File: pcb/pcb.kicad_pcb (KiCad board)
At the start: 2 copper layers, 57 parts, among them J1 AMT0440007DB0000G, J10 Conn_02x10_Counter_Clockwise, J11 Conn_01x03, J12 Conn_01x02, J15 Conn_01x10, J16 Conn_01x10, J2 AMT0440007DB0000G, J3 AMT0440007DB0000G, J4 AMT0440007DB0000G, J5 Conn_01x03, J6 Conn_01x03, J7 Conn_01x03, J8 Conn_01x03, J9 Conn_01x03, Q1 IRF9Z34NPBF, Q2 IRF9Z34NPBF, Q3 IRF9Z34NPBF, Q4 IRF9Z34NPBF, Q5 IRF9Z34NPBF, U1 ACS711ELCTR-12AB-T, U2 ACS711ELCTR-12AB-T, U3 ACS711ELCTR-12AB-T, U4 ACS711ELCTR-12AB-T, U5 ACS711ELCTR-12AB-T, U6 TXS0102DCUR, U7 TXS0102DCUR, U8 TXS0102DCUR, U9 NCP718BSNADJT1G

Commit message: Change C1 to be THT electrolytic instead of SMT
C1 is the largest filtering capacitor, which is used for the power
supply. It was previously an 0805 surface mount footprint. Changing it
to a through hole footprint gives us more flexibility if we need a
diferent capacitance.
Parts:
- C1: footprint Capacitor_SMD:C_0805_2012Metric_Pad1.18x1.45mm_HandSolder -> Capacitor_THT:C_Radial_D6.3mm_H11.0mm_P2.50mm
- moved C2 155.4 mm to (109.5, 131.0)
- moved C3 155.4 mm to (109.5, 134.0)
- moved C4 155.4 mm to (109.5, 137.0)
- moved C5 155.4 mm to (109.5, 140.0)
- moved C6 155.4 mm to (109.5, 143.0)
- moved R1 149.7 mm to (101.5, 131.1)
- moved R2 149.7 mm to (101.5, 134.1)
- moved R3 149.7 mm to (101.5, 137.0)
- moved R5 149.7 mm to (101.5, 142.9)
- moved R4 149.7 mm to (101.5, 139.9)
- moved R10 119.6 mm to (120.5, 75.6)
- moved R11 119.6 mm to (120.5, 78.5)
- moved R12 119.6 mm to (120.5, 81.5)
- moved R8 119.6 mm to (120.5, 69.7)
- moved R9 119.6 mm to (120.5, 72.7)
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
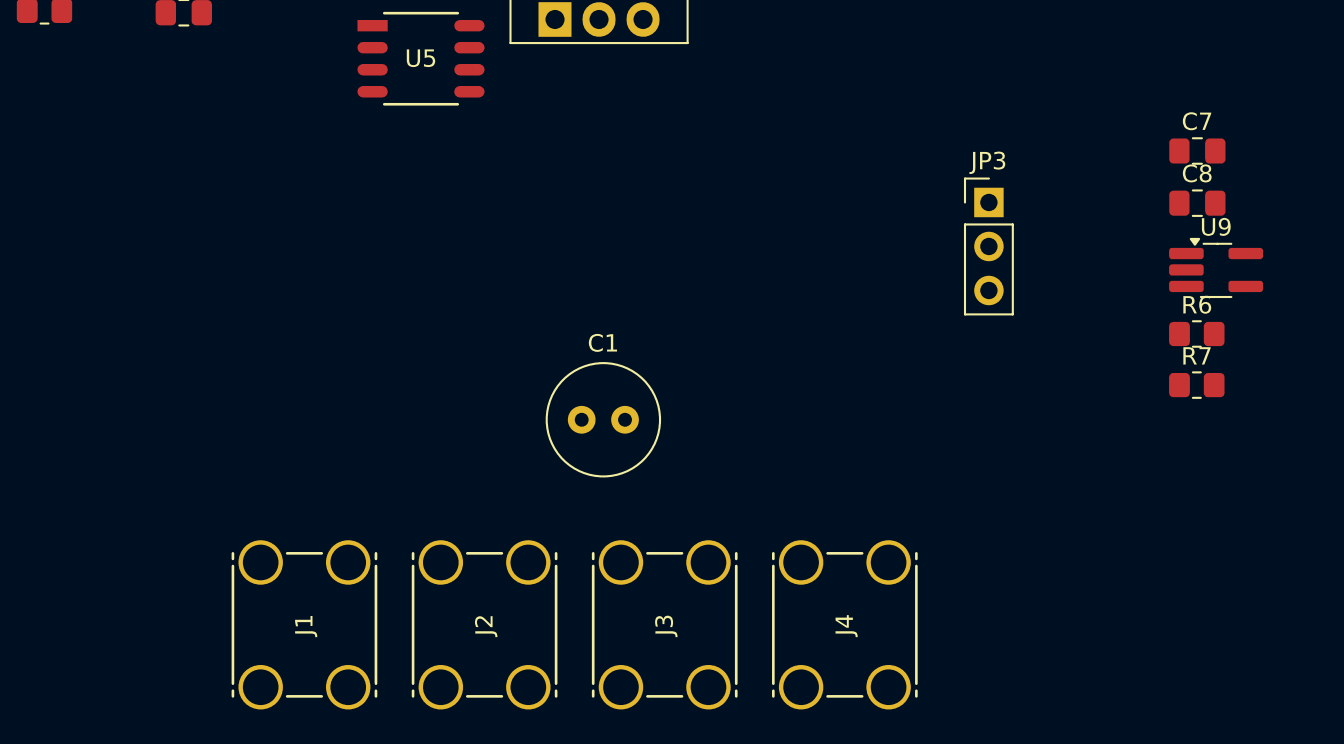
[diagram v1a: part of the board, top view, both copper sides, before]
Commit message: Add general 5V regulator layout
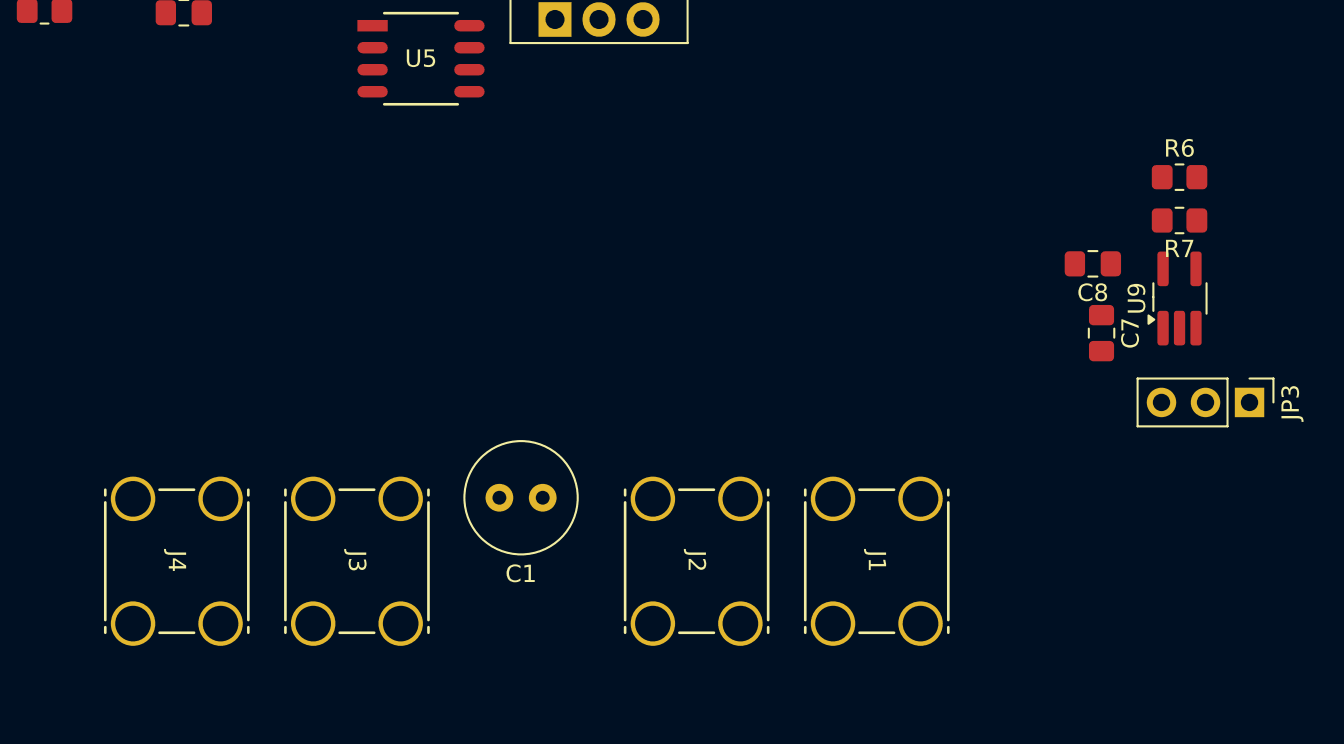
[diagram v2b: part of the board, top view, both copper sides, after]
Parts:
- moved J1 39.6 mm to (152.1, 171.1), turned to -90 degrees
- moved J4 35.2 mm to (111.7, 171.1), turned to -90 degrees
- moved J2 20.4 mm to (141.7, 171.1), turned to -90 degrees
- moved JP3 19.0 mm to (171.0, 165.5), turned to -90 degrees
- moved J3 16.7 mm to (122.1, 171.1), turned to -90 degrees
- moved C7 11.9 mm to (162.5, 161.5), turned to -90 degrees
- moved R7 9.55 mm to (167.0, 155.0), turned to 180 degrees
- moved R6 9.11 mm to (167.0, 152.5)
- moved C8 6.97 mm to (162.0, 157.5), turned to 180 degrees
- moved C1 5.03 mm to (130.2, 171.0), turned to 180 degrees
- moved U9 2.68 mm to (167.0, 159.5), turned to 90 degrees

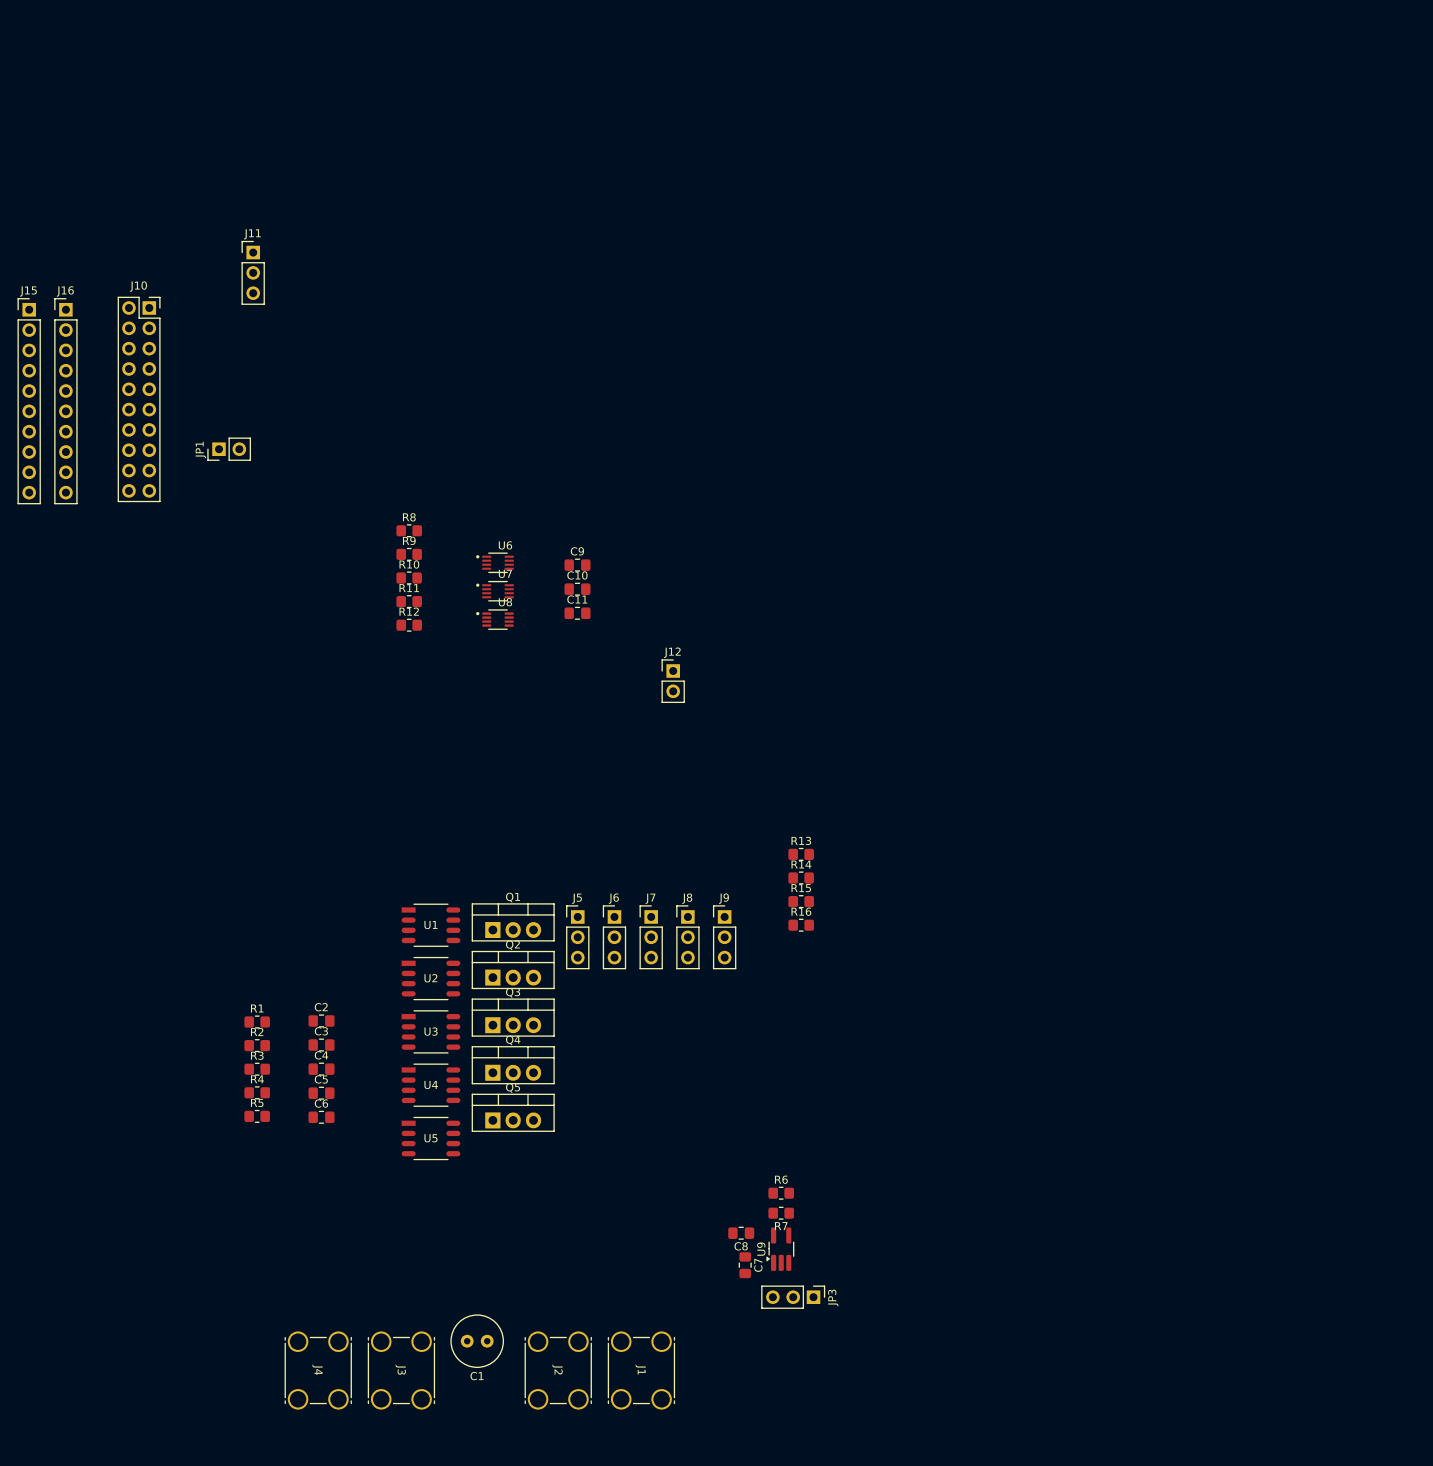
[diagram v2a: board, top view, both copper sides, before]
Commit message: Add general Hall effect sensor layout
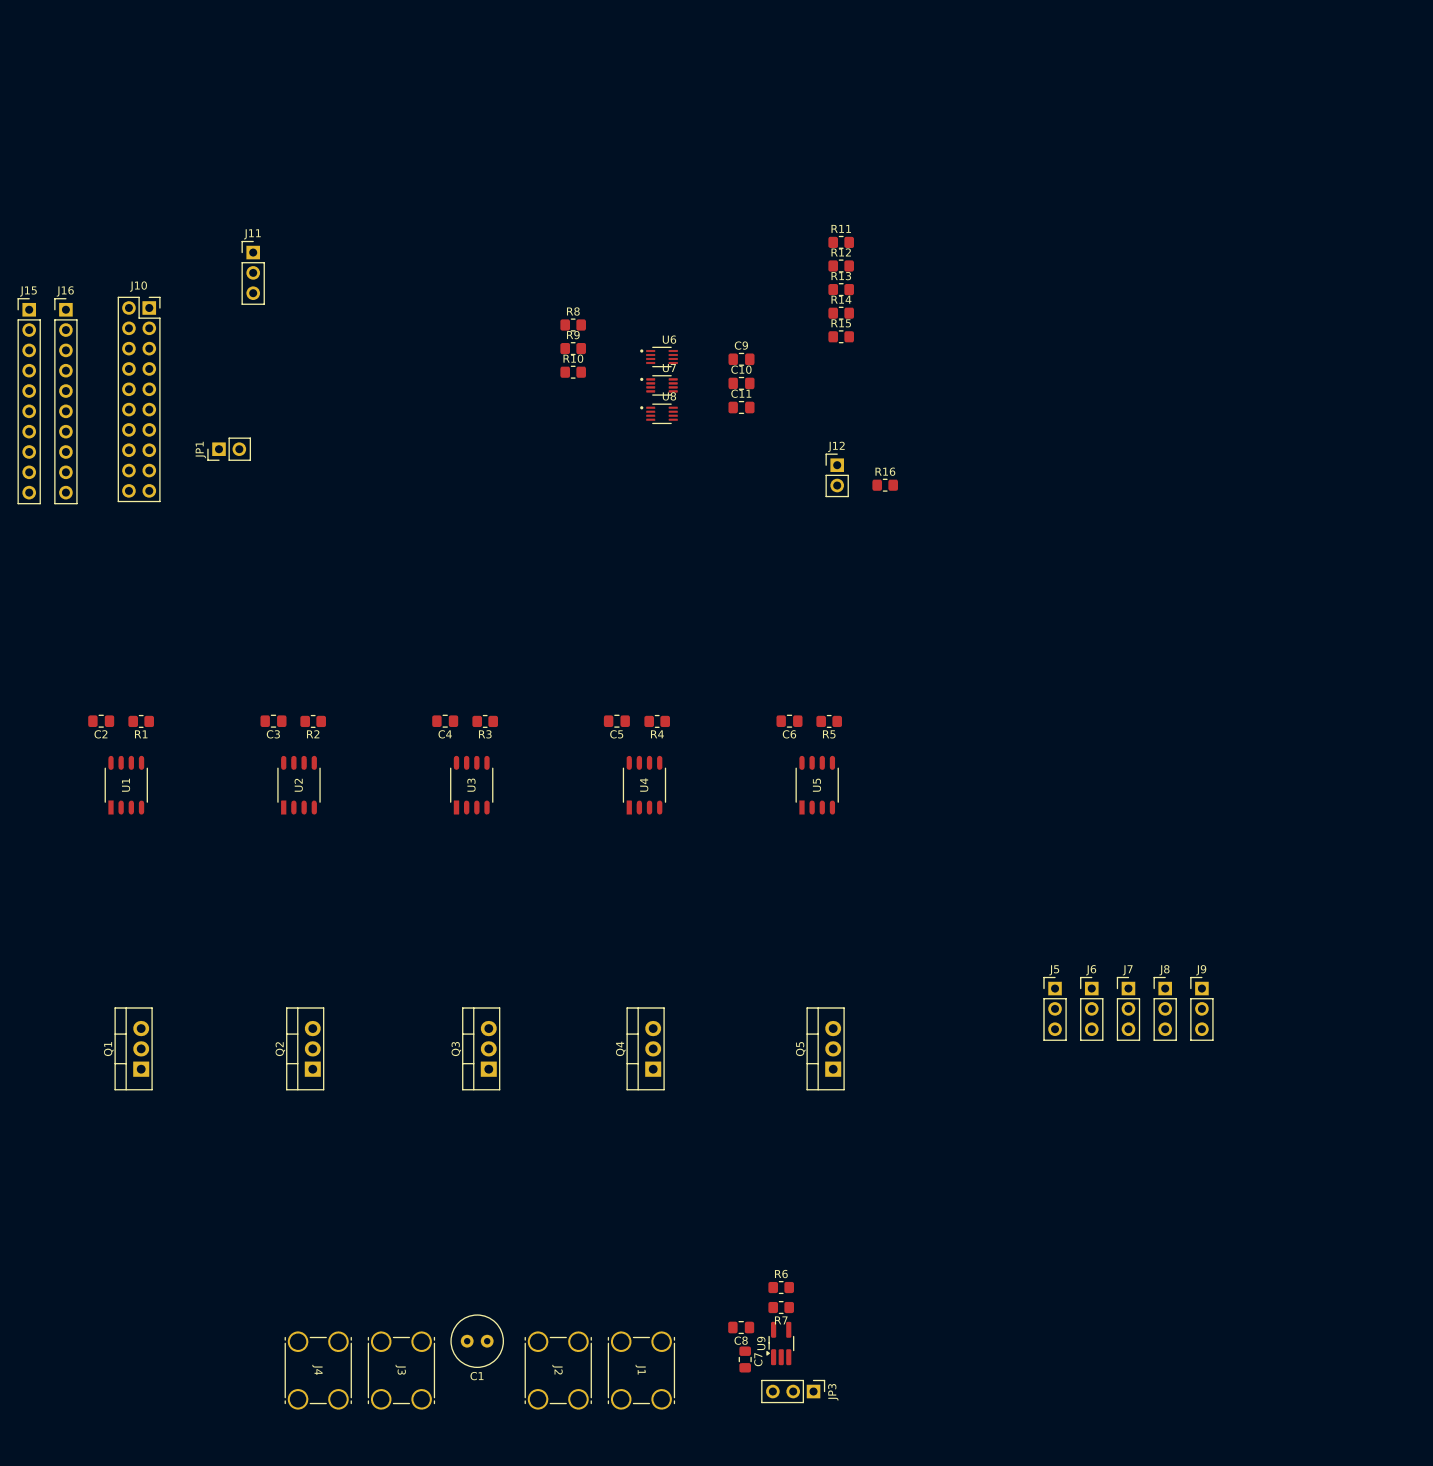
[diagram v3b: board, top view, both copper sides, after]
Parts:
- moved R5 86.9 mm to (173.0, 93.5), turned to 180 degrees
- moved C6 76.6 mm to (168.0, 93.5), turned to 180 degrees
- moved R13 70.8 mm to (174.5, 39.5)
- moved R14 70.8 mm to (174.5, 42.5)
- moved R15 70.8 mm to (174.5, 45.5)
- moved R11 70.2 mm to (174.5, 33.6)
- moved R12 70.2 mm to (174.5, 36.6)
- moved R4 68.2 mm to (151.5, 93.5), turned to 180 degrees
- moved U5 65.4 mm to (171.5, 101.5), turned to 90 degrees
- moved J5 60.3 mm to (201.2, 126.9)
- moved J6 60.3 mm to (205.8, 126.9)
- moved J7 60.3 mm to (210.4, 126.9)
- moved J8 60.3 mm to (215.0, 126.9)
- moved J9 60.3 mm to (219.6, 126.9)
- moved C5 59.4 mm to (146.5, 93.5), turned to 180 degrees
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
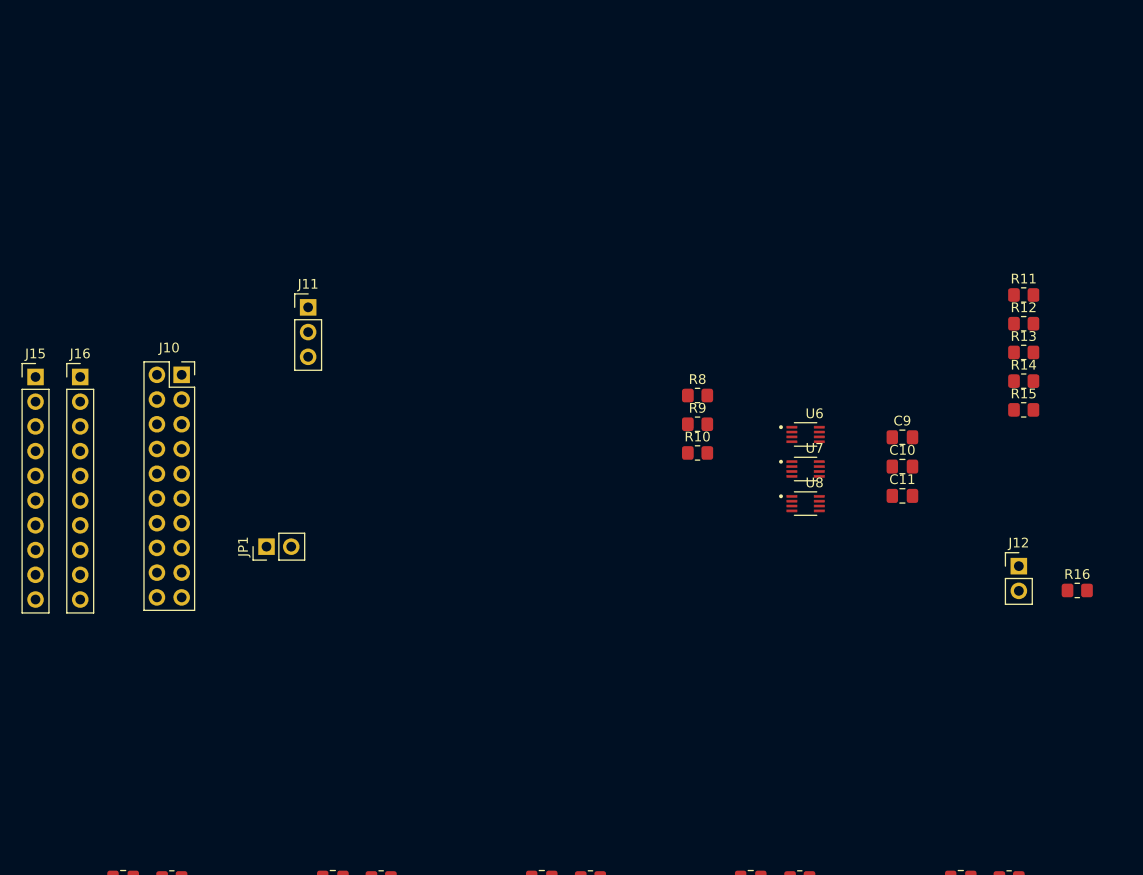
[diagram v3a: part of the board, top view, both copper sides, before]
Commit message: Add general level shifter layout
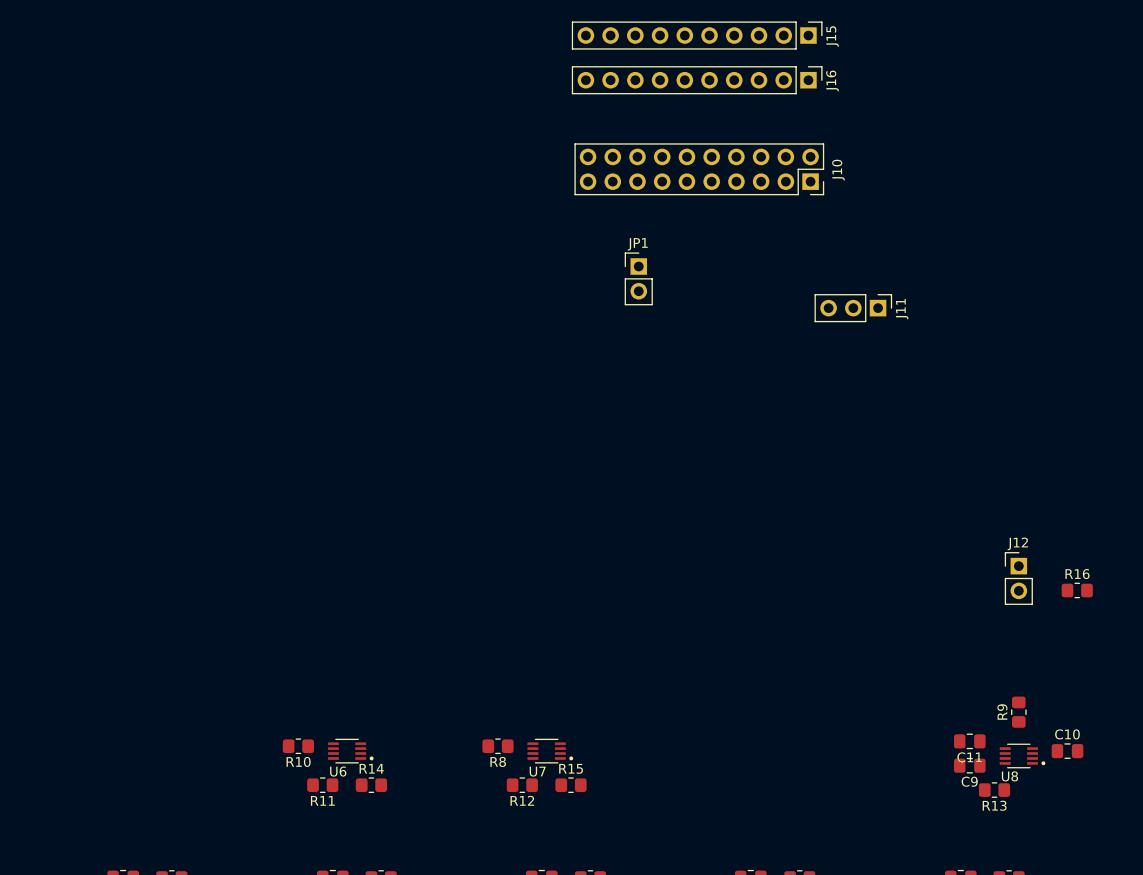
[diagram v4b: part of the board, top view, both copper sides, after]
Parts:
- moved R11 87.9 mm to (102.5, 84.0), turned to 180 degrees
- moved J15 86.8 mm to (152.4, 7.00), turned to -90 degrees
- moved J16 80.8 mm to (152.4, 11.6), turned to -90 degrees
- moved R14 78.8 mm to (107.5, 84.0)
- moved R12 70.0 mm to (123.0, 84.0), turned to 180 degrees
- moved J10 67.6 mm to (152.6, 22.0), turned to -90 degrees
- moved R15 60.4 mm to (128.0, 84.0)
- moved J11 58.5 mm to (159.5, 35.0), turned to -90 degrees
- moved U6 57.2 mm to (105.0, 80.5), turned to 180 degrees
- moved R10 50.9 mm to (100.0, 80.0), turned to 180 degrees
- moved JP1 47.9 mm to (135.0, 30.7), turned to 0 degrees
- moved R13 45.1 mm to (171.5, 84.5), turned to 180 degrees
- moved R9 44.3 mm to (174.0, 76.5), turned to 90 degrees
- moved R8 41.4 mm to (120.5, 80.0), turned to 180 degrees
- moved U7 39.3 mm to (125.5, 80.5), turned to 180 degrees
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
